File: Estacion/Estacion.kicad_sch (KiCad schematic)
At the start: 7 parts, among them U4 WeMos_S2_mini, U5 DHT22, U6 FN-M16P

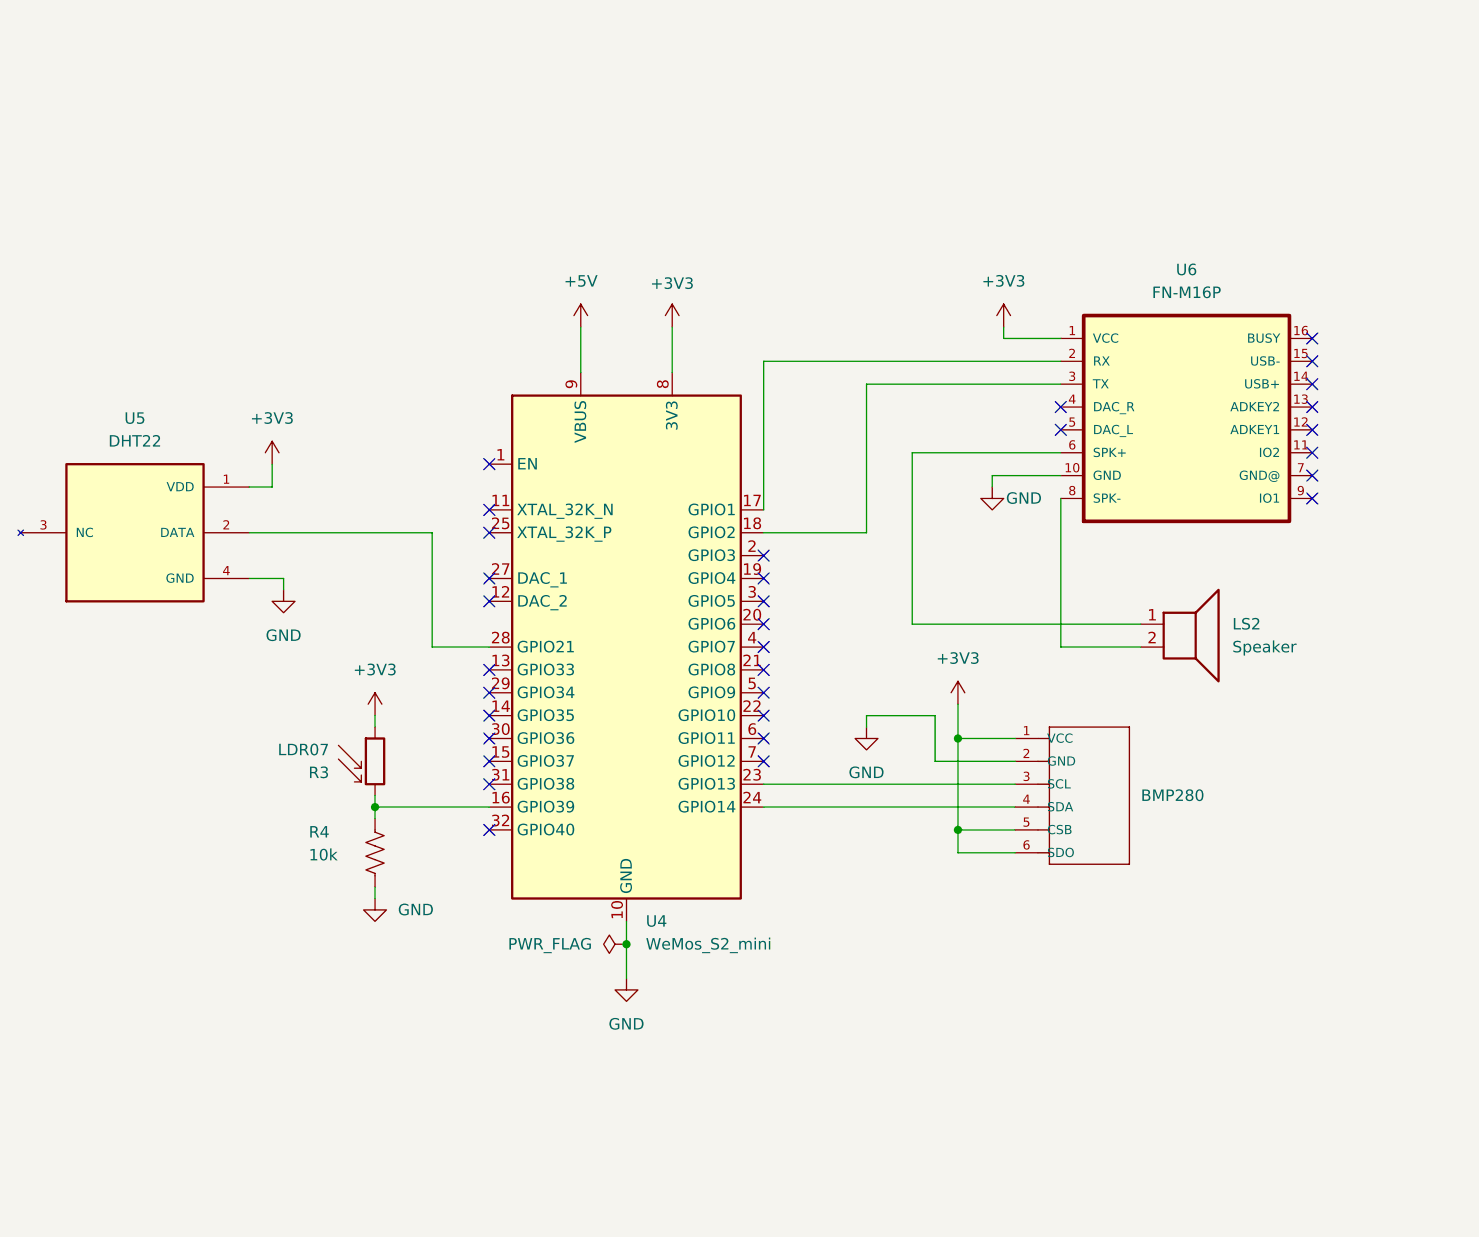
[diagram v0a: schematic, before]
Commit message: terminar pantalla y leds
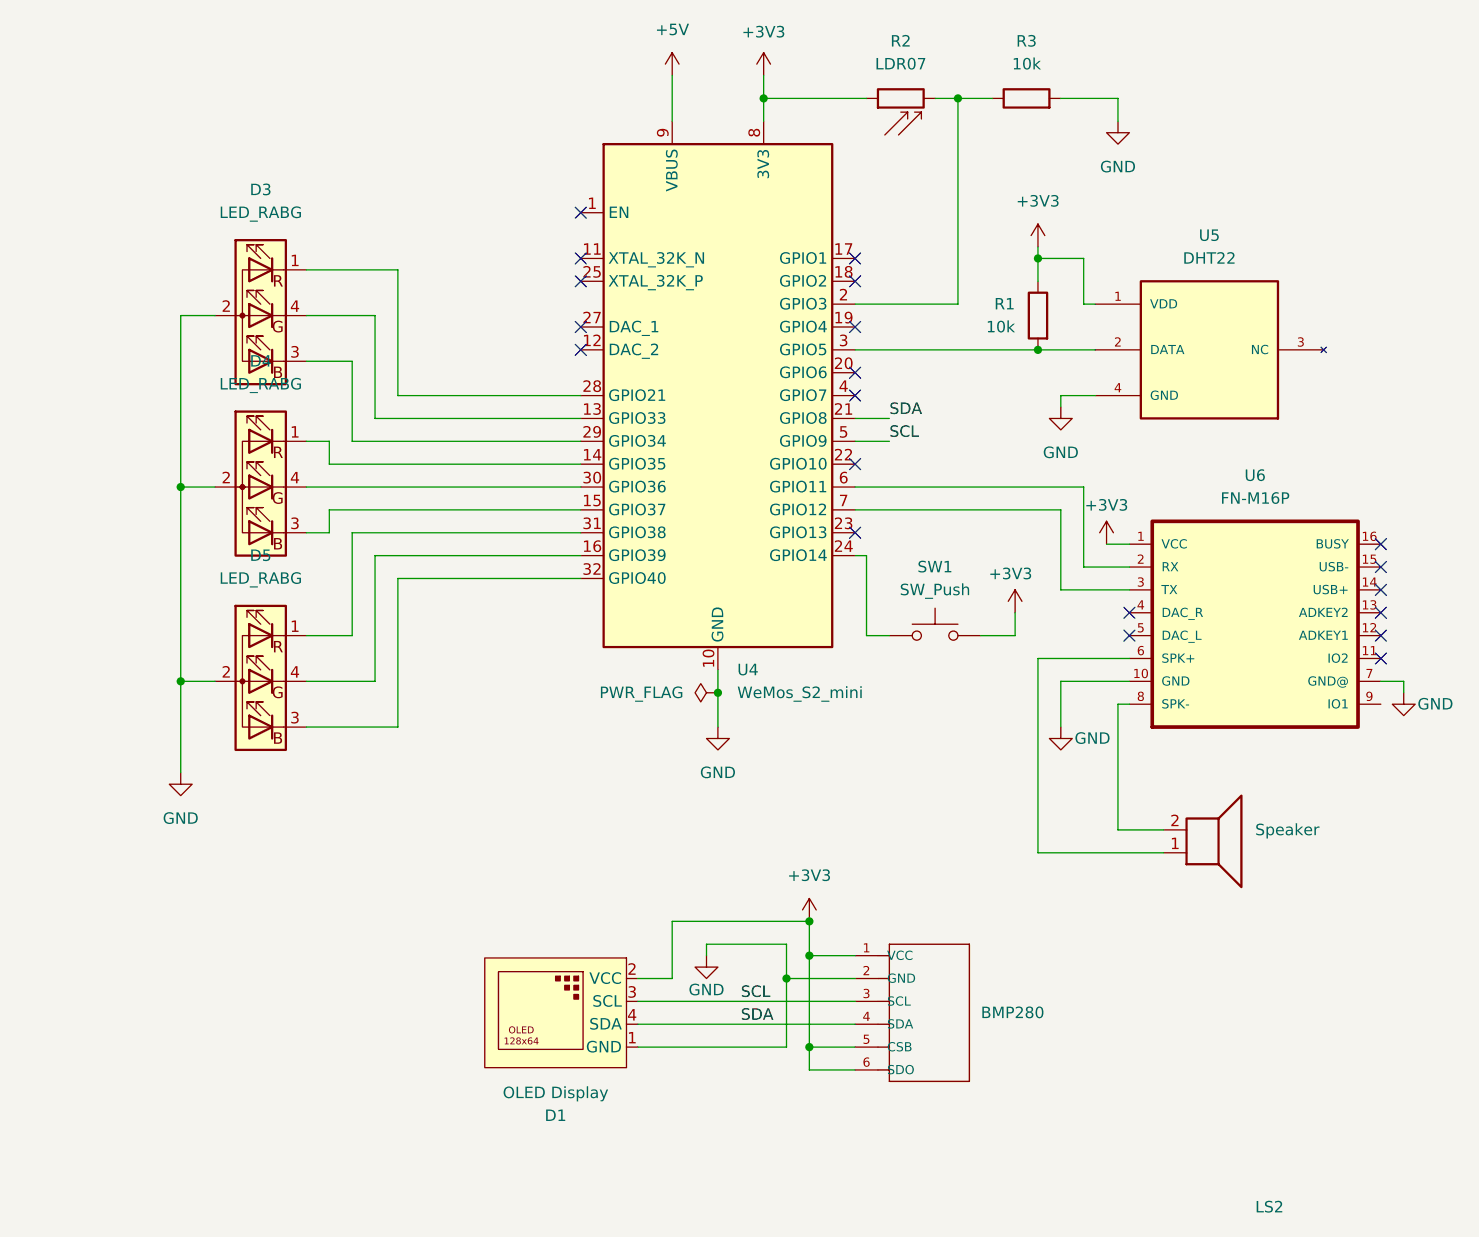
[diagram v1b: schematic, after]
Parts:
- removed R3: LDR07, OptoDevice:R_LDR_5.1x4.3mm_P3.4mm_Vertical, symbol Sensor_Optical:LDR07
- removed R4: 10k, Resistor_THT:R_Axial_DIN0204_L3.6mm_D1.6mm_P5.08mm_Horizontal, symbol Device:R_US
- added D1: OLED Display, especificos:OLED-Display_SSD1306_128x64, symbol Display:OLED_Display128x64
- added D3, D4, D5: LED_RABG, LED_THT:LED_D5.0mm-4_RGB, symbol Device:LED_RABG
- added R1, R3: 10k, Resistor_SMD:R_1206_3216Metric_Pad1.30x1.75mm_HandSolder, symbol Device:R
- added R2: LDR07, OptoDevice:R_LDR_5.1x4.3mm_P3.4mm_Vertical, symbol Sensor_Optical:LDR07
- added SW1: SW_Push, Button_Switch_THT:SW_PUSH_6mm, symbol Switch:SW_Push
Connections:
- net +3V3: now also D1.2 (VCC), R1.1, R2.1, SW1.1
- net GND: now also U6.7 (GND@), D1.1 (GND), D3.2 (A), D4.2 (A), D5.2 (A), R3.2
- net at U4.13 (GPIO33): now also D3.4 (GK)
- net at U4.14 (GPIO35): now also D4.1 (RK)
- net at U4.15 (GPIO37): now also D4.3 (BK)
- net at U4.16 (GPIO39): now also D5.4 (GK)
- net at U4.17 (GPIO1): no longer U6.2 (RX)
- net at U4.18 (GPIO2): no longer U6.3 (TX)
- net at U4.2 (GPIO3): now also R2.2, R3.1
- net SDA: now reaches U4.21 (GPIO8)
- net SDA: now also BMP280.4 (SDA), D1.4 (SDA)
- net at U4.23 (GPIO13): no longer BMP280.3 (SCL)
- net at U4.24 (GPIO14): now also SW1.2; no longer BMP280.4 (SDA)
- net at U4.28 (GPIO21): now also D3.1 (RK); no longer U5.2 (DATA)
- net at U4.29 (GPIO34): now also D3.3 (BK)
- net at U4.3 (GPIO5): now also U5.2 (DATA), R1.2
- net at U4.30 (GPIO36): now also D4.4 (GK)
- net at U4.31 (GPIO38): now also D5.1 (RK)
- net at U4.32 (GPIO40): now also D5.3 (BK)
- net SCL: now reaches U4.5 (GPIO9)
- net SCL: now also BMP280.3 (SCL), D1.3 (SCL)
- net at U4.6 (GPIO11): now also U6.2 (RX)
- net at U4.7 (GPIO12): now also U6.3 (TX)
- no-connect marks 32 -> 20
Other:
- moved on the sheet: BMP280, LS2, U4, U5, U6
